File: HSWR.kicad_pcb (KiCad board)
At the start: 4 copper layers, 152 x 139 mm, 158 parts, among them IC1 B1212S-2W, IC2 JW5052C, IC3 JW5052C, IC4 ADUM3054, IC5 ADuM4160, J1 USB_B, J2 IO, J3 B+, J4 B-, J5 U, J6 V, J7 W, J8 SWD, J9 AVR-ISP-6, Q1 IXFK300N20X3, Q2 IXFK300N20X3, Q3 IXFK300N20X3, Q4 IXFK300N20X3, Q5 IXFK300N20X3, Q6 IXFK300N20X3, Q7 Q_NMOS_GSD, U1 ACS781xLRTR-150B, U10 AM26LV32xD, U11 ADuM120N, U12 ADuM120N, U13 PC355, U2 ACS781xLRTR-150B, U3 ACS781xLRTR-150B, U4 STM32F405RGTx, U5 IRS2186, U6 IRS2186, U7 IRS2186, U8 AP1117-50, U9 ATtiny13A-SU, Y1 8MHz

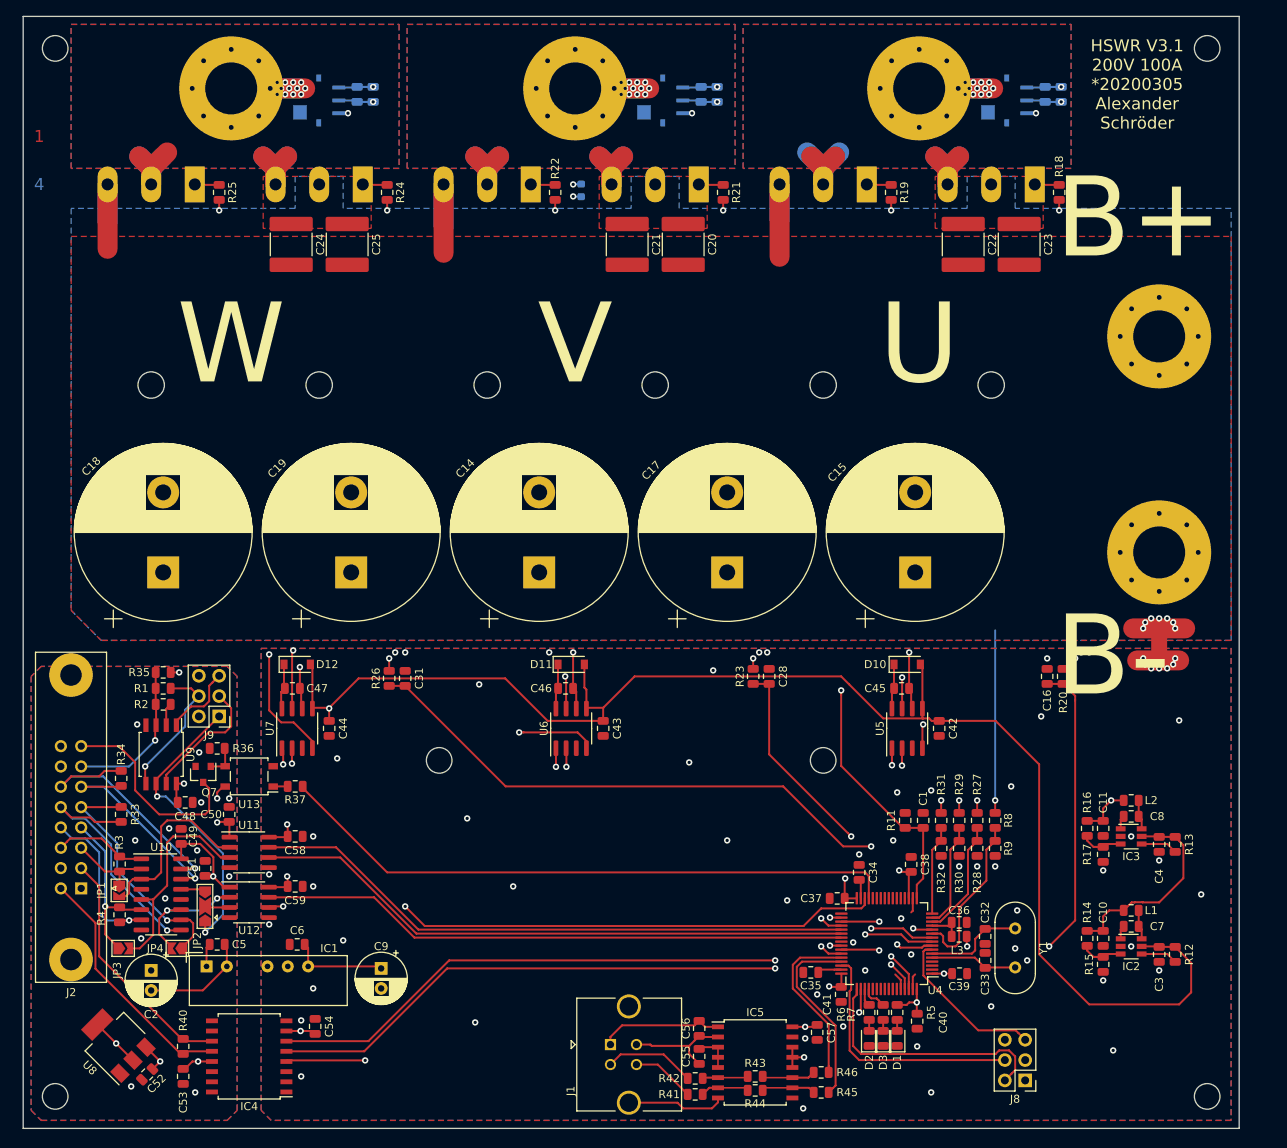
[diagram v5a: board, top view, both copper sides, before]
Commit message: - enlarged isolated island - bigger package for fan MOSFET - added 12V input protection - added U_DC sensing filter - added M_temp input filter - added reset pin decoupling for AVR - added HALL pull-ups - added TRI state selector jumper for buffer - removed UART selector jumper (AVR will check and switch to TRI state if needed)
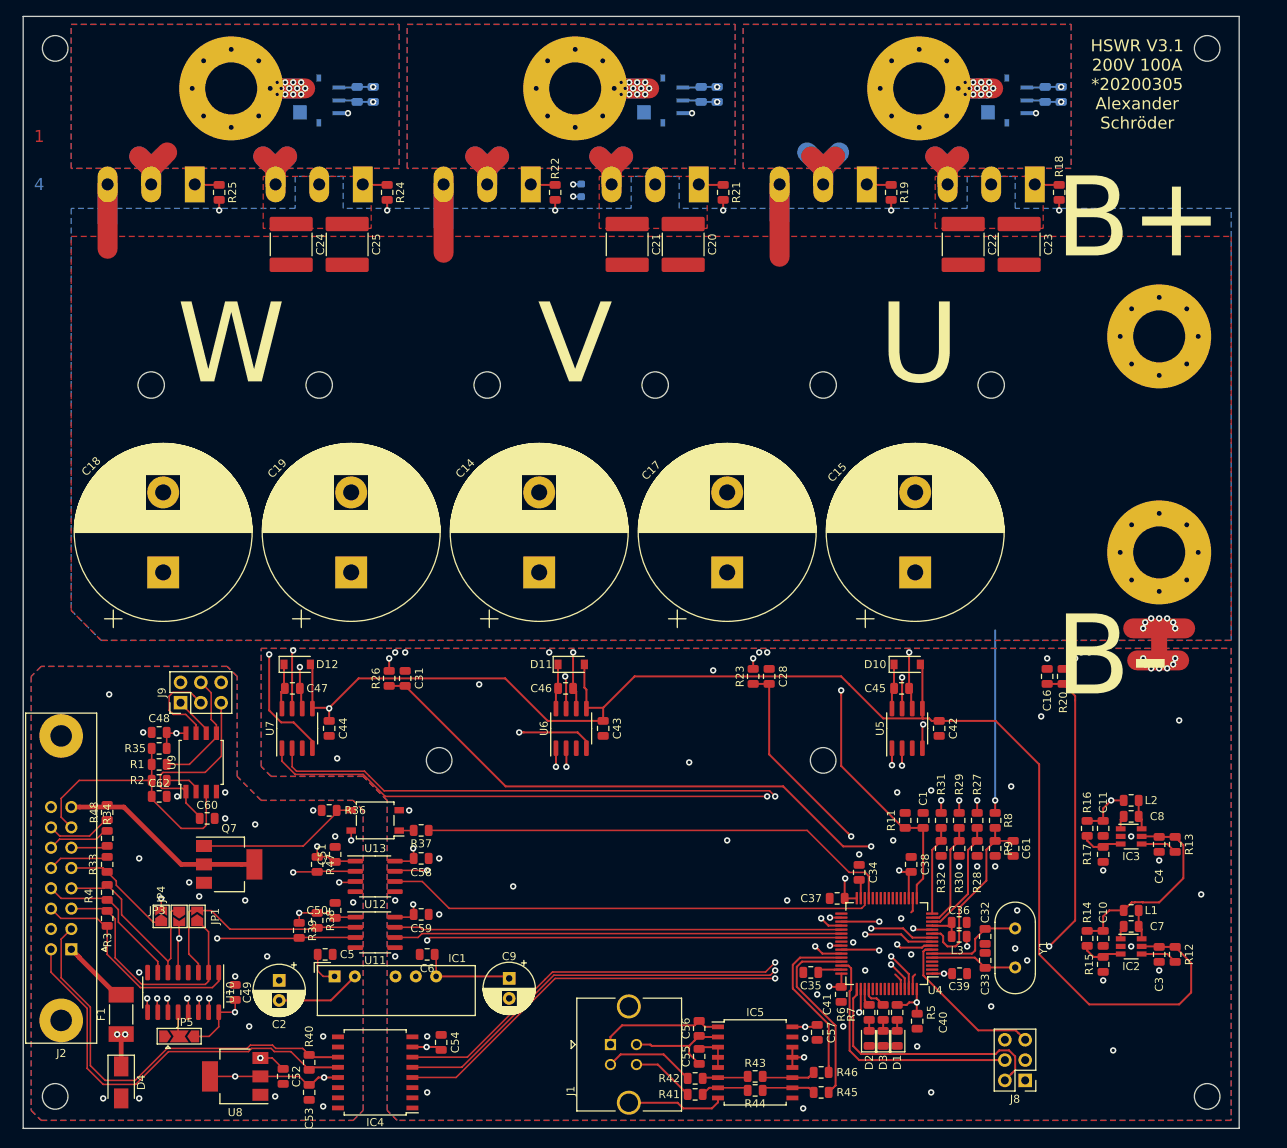
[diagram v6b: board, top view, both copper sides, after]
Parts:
- removed JP2: UART, Jumper:SolderJumper-3_P2.0mm_Open_TrianglePad1.0x1.5mm
- added C60: 10n, Capacitor_SMD:C_0805_2012Metric, F.Cu at (90.0, 124.2)
- added C61: 1u, Capacitor_SMD:C_0805_2012Metric, F.Cu at (190.8, 128.0)
- added C62: 10n, Capacitor_SMD:C_0805_2012Metric, F.Cu at (84.0, 121.5)
- added D4: 12V, Diode_SMD:D_SMA, F.Cu at (79.2, 157.2)
- added F1: 1A, Fuse:Fuse_Littelfuse-NANO2-451_453, F.Cu at (79.2, 148.8)
- added JP5: EN, Jumper:SolderJumper-3_P2.0mm_Open_TrianglePad1.0x1.5mm, F.Cu at (86.5, 151.5)
- added R38: 1k, Resistor_SMD:R_0805_2012Metric, F.Cu at (103.8, 137.0)
- added R39: 1k, Resistor_SMD:R_0805_2012Metric, F.Cu at (101.5, 138.2)
- added R47: 1k, Resistor_SMD:R_0805_2012Metric, F.Cu at (103.8, 130.0)
- added R48: 10k, Resistor_SMD:R_0805_2012Metric, F.Cu at (77.5, 123.5)
- Q7: value Q_NMOS_GSD -> Q_NMOS_GDS; footprint Package_TO_SOT_SMD:SOT-23 -> Package_TO_SOT_SMD:SOT-223-3_TabPin2
- moved C49 20.6 mm to (93.5, 146.0)
- moved U11 18.7 mm to (111.0, 138.5)
- moved C50 17.9 mm to (106.0, 135.8)
- moved C52 17.0 mm to (99.5, 156.5), turned to 270 degrees
- moved R37 16.7 mm to (116.8, 125.8)
- moved U13 16.7 mm to (111.0, 124.5)
- moved C51 16.3 mm to (106.0, 128.8)
- moved C6 16.3 mm to (117.5, 141.2)
- moved C59 16.1 mm to (116.8, 136.2)
- moved U12 16.1 mm to (111.0, 131.5)
- moved C2 16.0 mm to (99.0, 144.5)
- moved C9 16.0 mm to (127.8, 144.2)
- moved IC1 16.0 mm to (105.9, 144.0)
- moved R36 16.0 mm to (105.2, 123.2)
- moved C58 16.0 mm to (116.8, 129.2)
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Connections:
- IC4 pad 10: Net-(IC4-Pad10) -> (no net)
- J2 pad 1: +12VA -> Net-(F1-Pad2)
- J8 pad 6: Net-(J8-Pad6) -> (no net)
- Q7 pad 2: Earth -> /iso IO/Fan_Out
- Q7 pad 3: /iso IO/Fan_Out -> Earth
- U1 pad 4: Net-(U1-Pad4) -> (no net)
- U1 pad 7: Net-(U1-Pad7) -> (no net)
- U10 pad 12: Earth -> Net-(JP5-Pad2)
- U10 pad 13: Net-(JP2-Pad3) -> Net-(J9-Pad1)
- U10 pad 4: Net-(U10-Pad4) -> (no net)
- U12 pad 3: Net-(JP2-Pad2) -> Net-(J9-Pad1)
- U2 pad 4: Net-(U2-Pad4) -> (no net)
- U2 pad 7: Net-(U2-Pad7) -> (no net)
- U3 pad 4: Net-(U3-Pad4) -> (no net)
- U3 pad 7: Net-(U3-Pad7) -> (no net)
- U4 pad 2: Net-(U4-Pad2) -> (no net)
- U4 pad 20: Net-(U4-Pad20) -> (no net)
- U4 pad 21: Net-(U4-Pad21) -> (no net)
- U4 pad 22: Net-(U4-Pad22) -> (no net)
- U4 pad 23: Net-(U4-Pad23) -> (no net)
- U4 pad 24: Net-(U4-Pad24) -> (no net)
- U4 pad 25: Net-(U4-Pad25) -> (no net)
- U4 pad 26: Net-(U4-Pad26) -> (no net)
- U4 pad 27: Net-(U4-Pad27) -> (no net)
- U4 pad 28: Net-(U4-Pad28) -> (no net)
- U4 pad 3: Net-(U4-Pad3) -> (no net)
- U4 pad 33: Net-(U4-Pad33) -> (no net)
- U4 pad 4: Net-(U4-Pad4) -> (no net)
- U4 pad 40: Net-(U4-Pad40) -> (no net)
- U4 pad 53: Net-(U4-Pad53) -> (no net)
- U4 pad 54: Net-(U4-Pad54) -> (no net)
- U4 pad 55: Net-(U4-Pad55) -> (no net)
- U4 pad 56: Net-(U4-Pad56) -> (no net)
- U4 pad 57: Net-(U4-Pad57) -> (no net)
- U4 pad 58: Net-(U4-Pad58) -> (no net)
- U4 pad 59: Net-(U4-Pad59) -> (no net)
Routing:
- net Net-(J9-Pad1): track 36.5 -> 62.8 mm
- net Net-(JP4-Pad2): track 16.0 -> 41.8 mm, vias 2 -> 3
- net /CAN bus transceiver/CANL: track 30.5 -> 53.3 mm
- net /iso IO/Hall_1A: track 10.5 -> 32.2 mm
- net /CAN bus transceiver/CANH: track 30.9 -> 52.1 mm
- net /MCU/HALL_1: track 75.8 -> 55.9 mm
- net /MCU/HALL_2: track 75.5 -> 56.0 mm
- net /MCU/Fan_CPU: track 78.3 -> 60.1 mm
- net /iso IO/Hall_1B: track 11.6 -> 28.5 mm
- net Net-(Q7-Pad1): track 4.06 -> 20.4 mm
- net /iso IO/UART: track 77.5 -> 61.2 mm, vias 2 -> 0
- net /iso IO/M_Temp: track 19.2 -> 35.4 mm, vias 1 -> 0
- net /MCU/CAN_VSS_SENSE: track 81.3 -> 65.7 mm
- net /CAN bus transceiver/CAN_RX: track 84.3 -> 68.9 mm
- net Net-(C60-Pad1): track 9.33 -> 24.3 mm
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
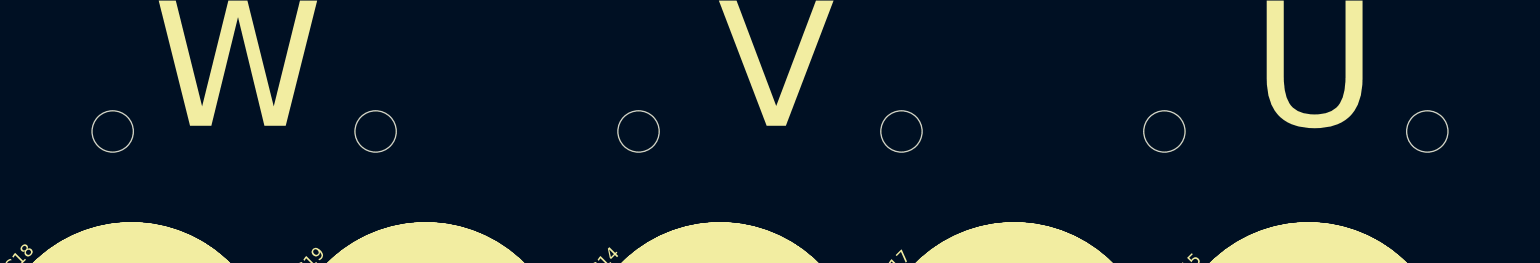
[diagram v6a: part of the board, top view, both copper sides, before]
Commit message: - specialized TO264 package for bigger screw hole
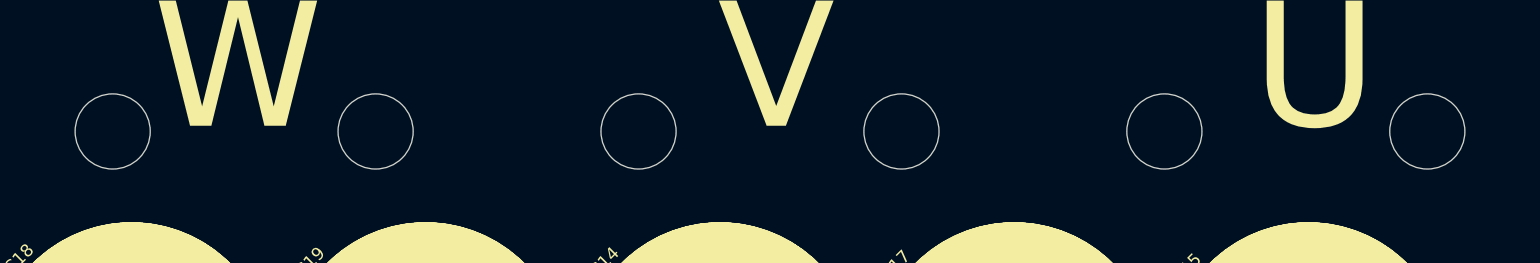
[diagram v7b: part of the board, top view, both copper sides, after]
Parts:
- Q1, Q2, Q3, Q4, Q5, Q6: footprint Package_TO_SOT_THT:TO-264-3_Horizontal_TabUp -> HSWR:TO-264-3_Horizontal_TabUp_6mm_hole

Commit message: - reworked silkscreen
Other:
- board text added: "HSWR V3.1 200V 100A *20200526 Alexander Schröder"
- board text removed: "HSWR V3.1 200V 100A *20200305 Alexander Schröder"
